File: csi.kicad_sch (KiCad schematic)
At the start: 61 parts, among them J7 WE_68715014522_ONE-SIDE, J8 WE_68715014522_ONE-SIDE, U24 AP22653FDZ-7, U25 AP22653FDZ-7, U26 PCA9547BS, U27 AP22653FDZ-7, U28 AP22653FDZ-7, U31 NTS0102GT, U32 NTS0102GT

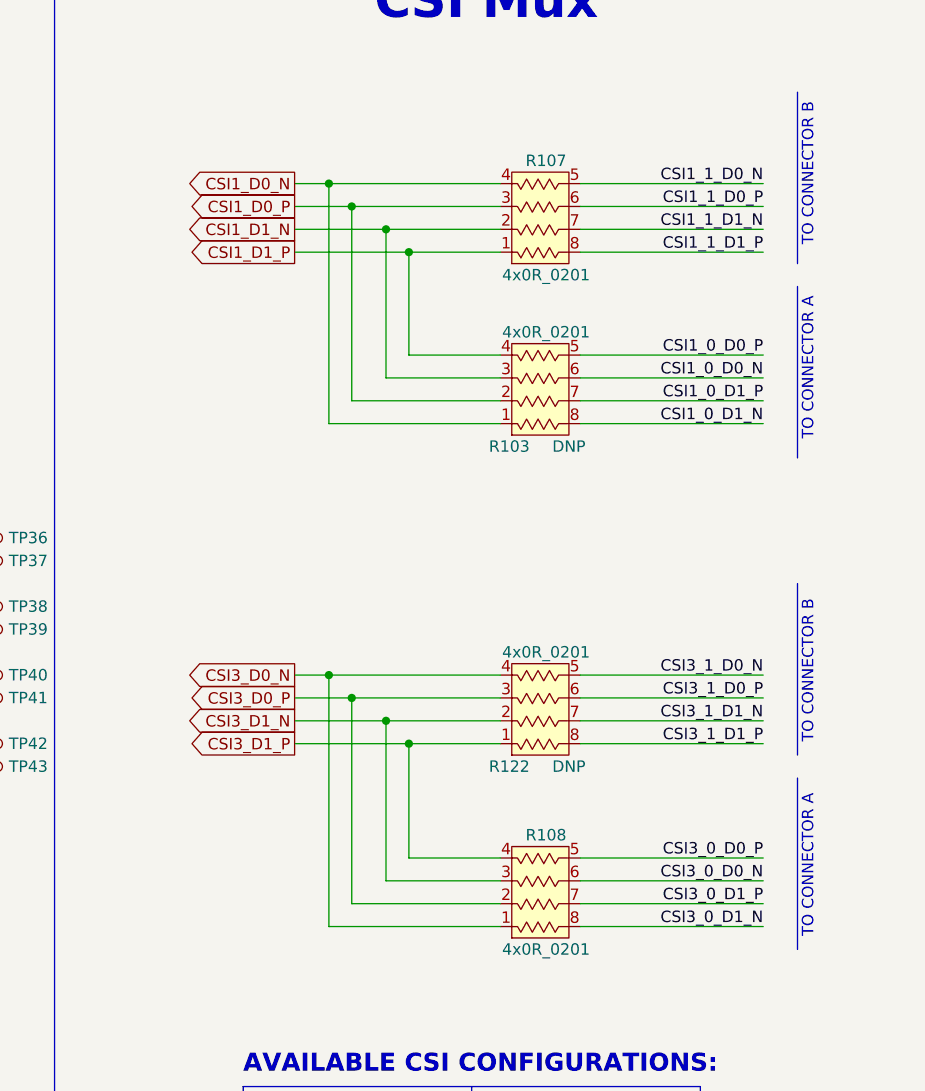
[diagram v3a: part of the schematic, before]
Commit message: Fixed swapped CSI signals
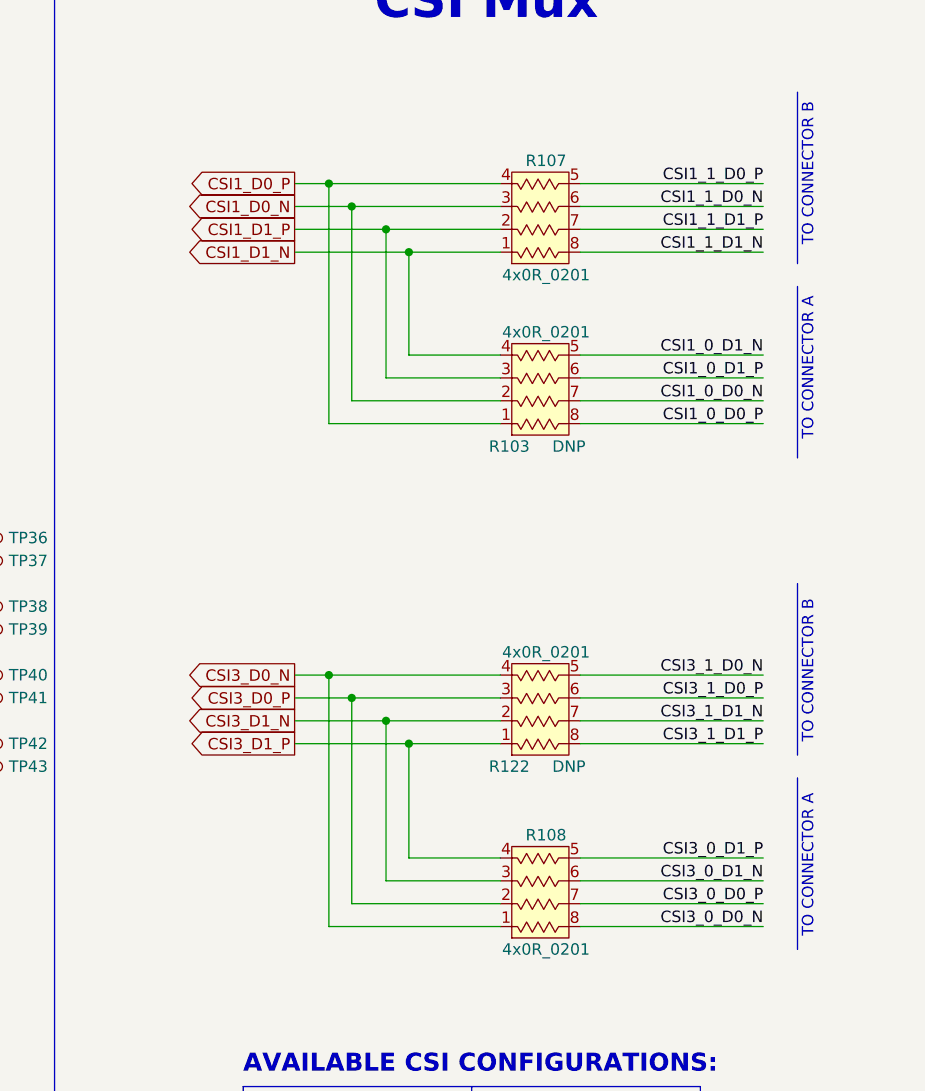
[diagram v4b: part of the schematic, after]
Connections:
- net CSI1_0_D0_N: now also R103.7; no longer R103.6
- net CSI1_0_D0_P: now also R103.8; no longer R103.5
- net CSI1_0_D1_N: now also R103.5; no longer R103.8
- net CSI1_0_D1_P: now also R103.6; no longer R103.7
- net CSI1_1_D0_N: now also R107.6; no longer R107.5
- net CSI1_1_D0_P: now also R107.5; no longer R107.6
- net CSI1_1_D1_N: now also R107.8; no longer R107.7
- net CSI1_1_D1_P: now also R107.7; no longer R107.8
- net CSI1_D0_N: now also R103.2, R107.3; no longer R103.1, R107.4
- net CSI1_D0_P: now also R103.1, R107.4; no longer R103.2, R107.3
- net CSI1_D1_N: now also R103.4, R107.1; no longer R103.3, R107.2
- net CSI1_D1_P: now also R103.3, R107.2; no longer R103.4, R107.1
- net CSI3_0_D0_N: now also R108.8; no longer R108.6
- net CSI3_0_D0_P: now also R108.7; no longer R108.5
- net CSI3_0_D1_N: now also R108.6; no longer R108.8
- net CSI3_0_D1_P: now also R108.5; no longer R108.7

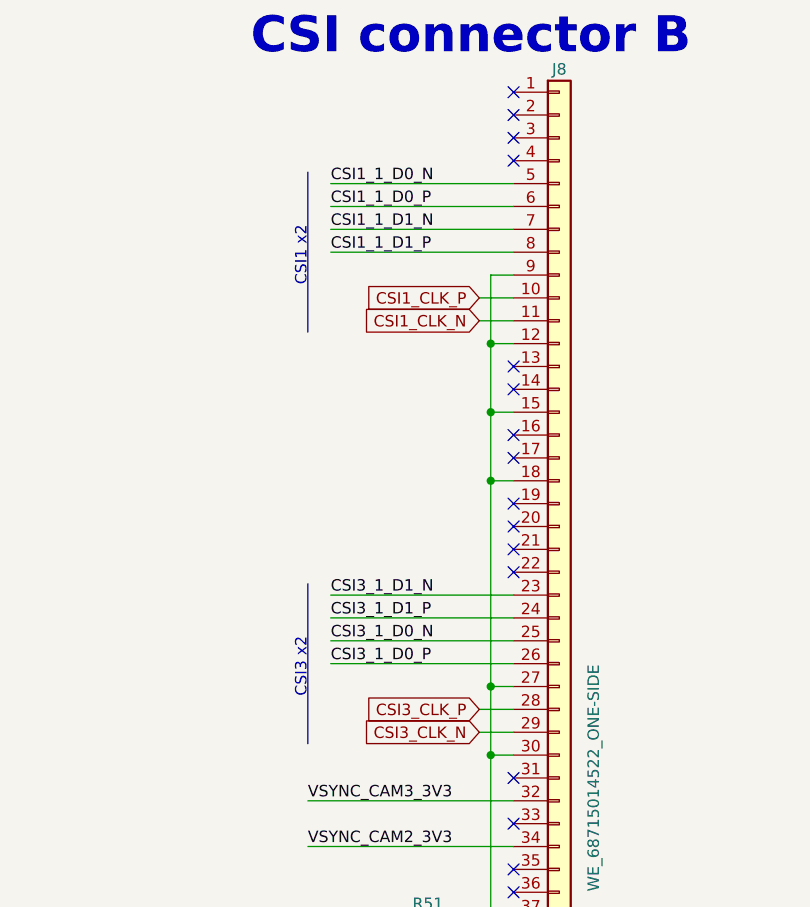
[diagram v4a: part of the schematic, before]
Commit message: Fixed bit order on CSI B connector
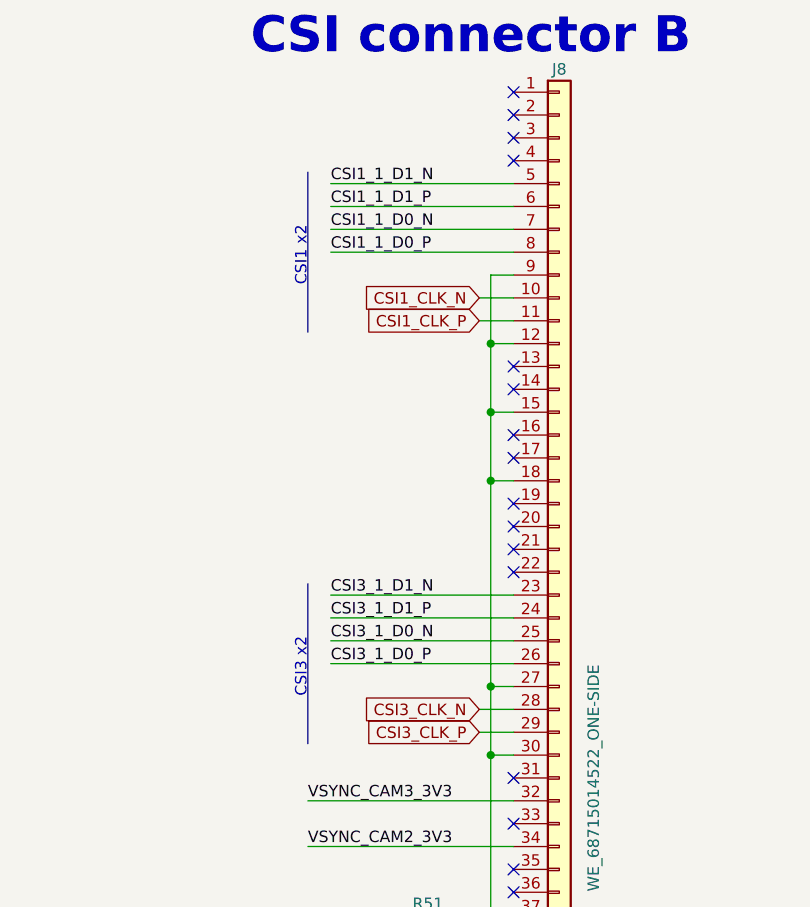
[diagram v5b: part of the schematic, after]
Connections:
- net CSI1_1_D0_N: now also J8.7 (Pin_7); no longer J8.5 (Pin_5)
- net CSI1_1_D0_P: now also J8.8 (Pin_8); no longer J8.6 (Pin_6)
- net CSI1_1_D1_N: now also J8.5 (Pin_5); no longer J8.7 (Pin_7)
- net CSI1_1_D1_P: now also J8.6 (Pin_6); no longer J8.8 (Pin_8)
- net CSI1_CLK_N: now also J8.10 (Pin_10); no longer J8.11 (Pin_11)
- net CSI1_CLK_P: now also J8.11 (Pin_11); no longer J8.10 (Pin_10)
- net CSI3_CLK_N: now also J8.28 (Pin_28); no longer J8.29 (Pin_29)
- net CSI3_CLK_P: now also J8.29 (Pin_29); no longer J8.28 (Pin_28)
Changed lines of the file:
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@@
     (effects (font (size 1.27 1.27)) (justify left bottom))
   )
-  (label "CSI1_1_D0_P" (at 342.9 35.56 0)
+  (label "CSI1_1_D0_P" (at 342.9 40.64 0)
     (effects (font (size 1.27 1.27)) (justify left bottom))
   )
@@
     (effects (font (size 1.27 1.27)) (justify left bottom))
   )
-  (label "CSI1_1_D1_N" (at 342.9 38.1 0)
+  (label "CSI1_1_D1_N" (at 342.9 33.02 0)
     (effects (font (size 1.27 1.27)) (justify left bottom))
   )
@@
     (effects (font (size 1.27 1.27)) (justify left bottom))
   )
-  (label "CSI1_1_D1_P" (at 342.9 40.64 0)
+  (label "CSI1_1_D1_P" (at 342.9 35.56 0)
     (effects (font (size 1.27 1.27)) (justify left bottom))
   )
@@
     (effects (font (size 1.27 1.27)) (justify left bottom))
   )
-  (label "CSI1_1_D0_N" (at 342.9 33.02 0)
+  (label "CSI1_1_D0_N" (at 342.9 38.1 0)
     (effects (font (size 1.27 1.27)) (justify left bottom))
   )
@@
     )
   )
-  (global_label "CSI1_CLK_P" (shape input) (at 359.41 45.72 180)
+  (global_label "CSI1_CLK_P" (shape input) (at 359.41 48.26 180)
+    (effects (font (size 1.27 1.27)) (justify right))
+    (property "Intersheet References" "${INTERSHEET_REFS}" (id 0) (at 345.44 48.26 0)
+      (effects (font (size 1.27 1.27)) (justify right))
+    )
+  )
+  (global_label "CSIA_PEN" (shape input) (at 90.17 213.36 180)
+    (effects (font (size 1.27 1.27)) (justify right))
+    (property "Intersheet References" "${INTERSHEET_REFS}" (id 0) (at 78.105 213.36 0)
+      (effects (font (size 1.27 1.27)) (justify right))
+    )
+  )
+  (global_label "CSI2_D0_N" (shape output) (at 280.67 83.82 180)
+    (effects (font (size 1.27 1.27)) (justify right))
+    (property "Intersheet References" "${INTERSHEET_REFS}" (id 0) (at 266.7 83.82 0)
+      (effects (font (size 1.27 1.27)) (justify right))
+    )
+  )
+  (global_label "CSI2_CLK_N" (shape input) (at 280.67 91.44 180)
+    (effects (font (size 1.27 1.27)) (justify right))
+    (property "Intersheet References" "${INTERSHEET_REFS}" (id 0) (at 266.7 91.44 0)
+      (effects (font (size 1.27 1.27)) (justify right))
+    )
+  )
+  (global_label "CSI1_CLK_N" (shape input) (at 359.41 45.72 180)
     (effects (font (size 1.27 1.27)) (justify right))
     (property "Intersheet References" "${INTERSHEET_REFS}" (id 0) (at 345.44 45.72 0)
@@
     )
   )
-  (global_label "CSIA_PEN" (shape input) (at 90.17 213.36 180)
-    (effects (font (size 1.27 1.27)) (justify right))
-    (property "Intersheet References" "${INTERSHEET_REFS}" (id 0) (at 78.105 213.36 0)
-      (effects (font (size 1.27 1.27)) (justify right))
-    )
-  )
-  (global_label "CSI2_D0_N" (shape output) (at 280.67 83.82 180)
-    (effects (font (size 1.27 1.27)) (justify right))
-    (property "Intersheet References" "${INTERSHEET_REFS}" (id 0) (at 266.7 83.82 0)
-      (effects (font (size 1.27 1.27)) (justify right))
-    )
-  )
-  (global_label "CSI2_CLK_N" (shape input) (at 280.67 91.44 180)
-    (effects (font (size 1.27 1.27)) (justify right))
-    (property "Intersheet References" "${INTERSHEET_REFS}" (id 0) (at 266.7 91.44 0)
-      (effects (font (size 1.27 1.27)) (justify right))
-    )
-  )
-  (global_label "CSI1_CLK_N" (shape input) (at 359.41 48.26 180)
-    (effects (font (size 1.27 1.27)) (justify right))
-    (property "Intersheet References" "${INTERSHEET_REFS}" (id 0) (at 345.44 48.26 0)
-      (effects (font (size 1.27 1.27)) (justify right))
-    )
-  )
   (global_label "CSI0_D1_N" (shape output) (at 280.67 33.02 180)
     (effects (font (size 1.27 1.27)) (justify right))
@@
     )
   )
-  (global_label "CSI3_CLK_N" (shape input) (at 359.41 93.98 180)
+  (global_label "CSI3_CLK_N" (shape input) (at 359.41 91.44 180)
+    (effects (font (size 1.27 1.27)) (justify right))
+    (property "Intersheet References" "${INTERSHEET_REFS}" (id 0) (at 345.44 91.44 0)
+      (effects (font (size 1.27 1.27)) (justify right))
+    )
+  )
+  (global_label "CSI3_CLK_P" (shape input) (at 359.41 93.98 180)
     (effects (font (size 1.27 1.27)) (justify right))
     (property "Intersheet References" "${INTERSHEET_REFS}" (id 0) (at 345.44 93.98 0)
       (effects (font (size 1.27 1.27)) (justify right))
     )
-  )
-  (global_label "CSI3_CLK_P" (shape input) (at 359.41 91.44 180)
-    (effects (font (size 1.27 1.27)) (justify right))
-    (property "Intersheet References" "${INTERSHEET_REFS}" (id 0) (at 345.44 91.44 0)
-      (effects (font (size 1.27 1.27)) (justify right))
-    )

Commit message: Loclib
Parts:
- C100, C101, C42, C43, C89, C90, C91, C96, C97: footprint antmicro-footprints:0402-cap -> jetson-orin-baseboard-footprints:0402-cap; symbol antmicroCapacitors0402:C_100n_0402 -> jetson-orin-baseboard:C_100n_0402
- C94, C95, C98, C99: footprint antmicro-footprints:0402-cap -> jetson-orin-baseboard-footprints:0402-cap; symbol antmicroCapacitors0402:C_1u_0402 -> jetson-orin-baseboard:C_1u_0402
- D18, D20, D24, D25: footprint antmicro-footprints:LED_0603 -> jetson-orin-baseboard-footprints:LED_0603; symbol antmicroLEDIndicationDiscrete:LTST-C190GKT -> jetson-orin-baseboard:LTST-C190GKT
- J7, J8: footprint antmicro-footprints:WE_68715014522_ONE-SIDE -> jetson-orin-baseboard-footprints:WE_68715014522_ONE-SIDE; symbol antmicroFCCConnectors:WE_68715014522_ONE-SIDE -> jetson-orin-baseboard:WE_68715014522_ONE-SIDE
- R10, R7, R8, R9: footprint antmicro-footprints:0402-res -> jetson-orin-baseboard-footprints:0402-res; symbol antmicroResistors0402:R_15k_0402 -> jetson-orin-baseboard:R_15k_0402
- R103, R107, R108, R122, R50, R51: footprint antmicro-footprints:EXB18V -> jetson-orin-baseboard-footprints:EXB18V; symbol antmicroResistorNetworksArrays:4x0R_0201_array -> jetson-orin-baseboard:4x0R_0201_array
- R132, R133: footprint antmicro-footprints:0402-res -> jetson-orin-baseboard-footprints:0402-res; symbol antmicroResistors0402:R_200R_0402 -> jetson-orin-baseboard:R_200R_0402
- R161, R162, R166, R167, R168, R171, R174, R179: footprint antmicro-footprints:0402-res -> jetson-orin-baseboard-footprints:0402-res; symbol antmicroResistors0402:R_0R_0402 -> jetson-orin-baseboard:R_0R_0402
- R163: footprint antmicro-footprints:0402-res -> jetson-orin-baseboard-footprints:0402-res; symbol antmicroResistors0402:R_10k_0402 -> jetson-orin-baseboard:R_10k_0402
- R180, R6: footprint antmicro-footprints:0402-res -> jetson-orin-baseboard-footprints:0402-res; symbol antmicroResistors0402:R_100k_0402 -> jetson-orin-baseboard:R_100k_0402
- R197, R206: footprint antmicro-footprints:0402-res -> jetson-orin-baseboard-footprints:0402-res; symbol antmicroResistors0402:R_470R_0402 -> jetson-orin-baseboard:R_470R_0402
- R36, R48: footprint antmicro-footprints:EXB18V -> jetson-orin-baseboard-footprints:EXB18V; symbol antmicroResistorNetworksArrays:4x2k2_0201_array -> jetson-orin-baseboard:4x2k2_0201_array
- TP36, TP37, TP38, TP39, TP40, TP41, TP42, TP43: footprint antmicro-footprints:Testpoint_smd_0_75mm -> jetson-orin-baseboard-footprints:Testpoint_smd_0_75mm; symbol antmicroTestPoints:TP_SMD_0_75MM -> jetson-orin-baseboard:TP_SMD_0_75MM
- U24, U25, U27, U28: footprint antmicro-footprints:DFN-6-1EP_2x2mm_P0.65mm_EP1x1.6mm -> jetson-orin-baseboard-footprints:DFN-6-1EP_2x2mm_P0.65mm_EP1x1.6mm; symbol antmicroPMICPowerDistributionSwitchesLoadDrivers:AP22653FDZ-7 -> jetson-orin-baseboard:AP22653FDZ-7
- U26: footprint antmicro-footprints:VQFN-24 -> jetson-orin-baseboard-footprints:VQFN-24; symbol antmicroLogicSignalSwitchesMultiplexersDecoders:PCA9547BS -> jetson-orin-baseboard:PCA9547BS
- U31, U32: footprint antmicro-footprints:PSON50P100X195X50-8N -> jetson-orin-baseboard-footprints:PSON50P100X195X50-8N; symbol antmicroLogicTranslatorsLevelShifters:NTS0102GT -> jetson-orin-baseboard:NTS0102GT
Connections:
- net CSI1_0_D0_N: no longer R103.7
- net CSI1_0_D0_P: no longer R103.8
- net CSI1_0_D1_N: no longer R103.5
- net CSI1_0_D1_P: no longer R103.6
- net CSI1_1_D0_N: no longer R107.6
- net CSI1_1_D0_P: no longer R107.5
- net CSI1_1_D1_N: no longer R107.8
- net CSI1_1_D1_P: no longer R107.7
- net CSI1_D0_N: no longer R103.2, R107.3
- net CSI1_D0_P: no longer R103.1, R107.4
- net CSI1_D1_N: no longer R103.4, R107.1
- net CSI1_D1_P: no longer R103.3, R107.2
- net CSI3_0_D0_N: no longer R108.8
- net CSI3_0_D0_P: no longer R108.7
- net CSI3_0_D1_N: no longer R108.6
- net CSI3_0_D1_P: no longer R108.5
- net CSI3_1_D0_N: no longer R122.5
- net CSI3_1_D0_P: no longer R122.6
- net CSI3_1_D1_N: no longer R122.7
- net CSI3_1_D1_P: no longer R122.8
- net CSI3_D0_N: no longer R108.1, R122.4
- net CSI3_D0_P: no longer R108.2, R122.3
- net CSI3_D1_N: no longer R108.3, R122.2
- net CSI3_D1_P: no longer R108.4, R122.1
- net SCL_CAM0: no longer R50.2
- net SCL_CAM1: no longer R50.4
- net SCL_CAM2: no longer R51.2
- net SCL_CAM3: no longer R51.4
- net SDA_CAM0: no longer R50.1
- net SDA_CAM1: no longer R50.3
- net SDA_CAM2: no longer R51.1
- net SDA_CAM3: no longer R51.3
- net at J8.39 (Pin_39): no longer R51.8
- net at J8.40 (Pin_40): no longer R51.7
- net at J8.41 (Pin_41): no longer R51.6
- net at J8.42 (Pin_42): no longer R51.5
- net at J7.42 (Pin_42): no longer R50.5
- net at J7.41 (Pin_41): no longer R50.6
- net at J7.40 (Pin_40): no longer R50.7
- net at J7.39 (Pin_39): no longer R50.8

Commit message: Fix symbols after loclib
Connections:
- net CSI1_0_D0_N: now also R103.7
- net CSI1_0_D0_P: now also R103.8
- net CSI1_0_D1_N: now also R103.5
- net CSI1_0_D1_P: now also R103.6
- net CSI1_1_D0_N: now also R107.6
- net CSI1_1_D0_P: now also R107.5
- net CSI1_1_D1_N: now also R107.8
- net CSI1_1_D1_P: now also R107.7
- net CSI1_D0_N: now also R103.2, R107.3
- net CSI1_D0_P: now also R103.1, R107.4
- net CSI1_D1_N: now also R103.4, R107.1
- net CSI1_D1_P: now also R103.3, R107.2
- net CSI3_0_D0_N: now also R108.8
- net CSI3_0_D0_P: now also R108.7
- net CSI3_0_D1_N: now also R108.6
- net CSI3_0_D1_P: now also R108.5
- net CSI3_1_D0_N: now also R122.5
- net CSI3_1_D0_P: now also R122.6
- net CSI3_1_D1_N: now also R122.7
- net CSI3_1_D1_P: now also R122.8
- net CSI3_D0_N: now also R108.1, R122.4
- net CSI3_D0_P: now also R108.2, R122.3
- net CSI3_D1_N: now also R108.3, R122.2
- net CSI3_D1_P: now also R108.4, R122.1
- net SCL_CAM0: now also R50.2
- net SCL_CAM1: now also R50.4
- net SCL_CAM2: now also R51.2
- net SCL_CAM3: now also R51.4
- net SDA_CAM0: now also R50.1
- net SDA_CAM1: now also R50.3
- net SDA_CAM2: now also R51.1
- net SDA_CAM3: now also R51.3
- net at J8.39 (Pin_39): now also R51.8
- net at J8.40 (Pin_40): now also R51.7
- net at J8.41 (Pin_41): now also R51.6
- net at J8.42 (Pin_42): now also R51.5
- net at J7.39 (Pin_39): now also R50.8
- net at J7.40 (Pin_40): now also R50.7
- net at J7.41 (Pin_41): now also R50.6
- net at J7.42 (Pin_42): now also R50.5
